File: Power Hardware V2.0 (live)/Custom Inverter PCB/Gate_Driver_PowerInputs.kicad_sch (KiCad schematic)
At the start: 22 parts, among them J1 1714971, J2 1714971, J3 1714968, J7 1714971, J8 1714971, K2 1-1393210-3, U1 DRV8300DIPWR

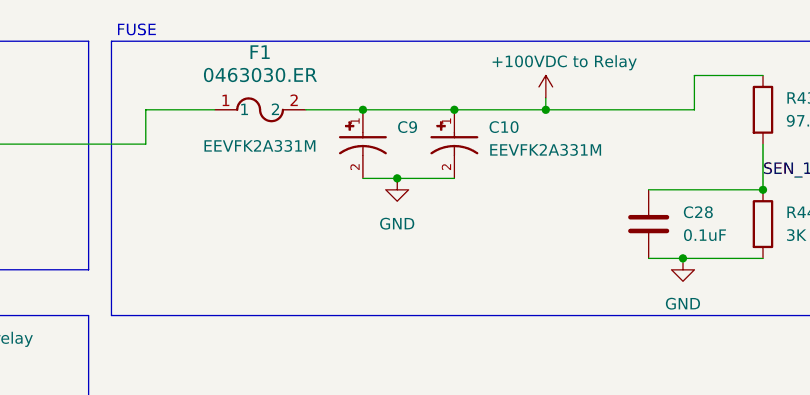
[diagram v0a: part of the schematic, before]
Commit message: footprint fixes
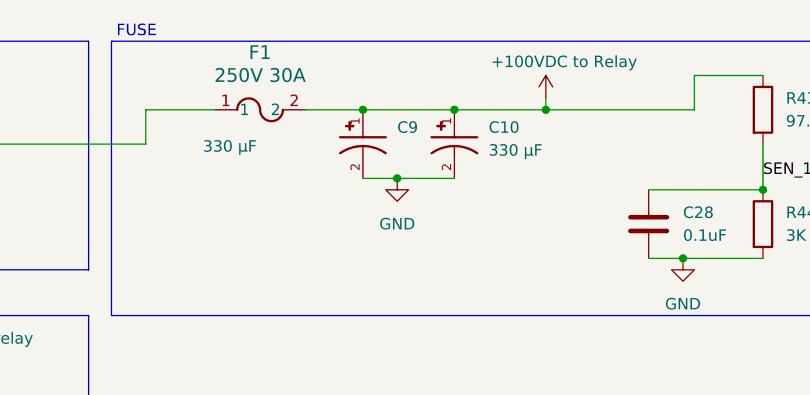
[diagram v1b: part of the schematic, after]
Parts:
- C10, C9: value EEVFK2A331M -> 330 µF; Part Number (none) -> EEVFK2A331M
- F1: value 0463030.ER -> 250V 30A; footprint 0463030ERFUSE:FUSE_0463_LTF-L -> 0463030_ER:FUSE_0463_LTF-M
- J3: footprint 1714968:PHOENIX_1714968 -> PHOENIX_1714968:PHOENIX_1714968
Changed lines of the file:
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@@
 			)
 		)
-		(property "Value" "EEVFK2A331M"
+		(property "Value" "330 µF"
 			(at 63.5 26.924 90)
 			(effects
@@
 			)
 		)
-		(property "Datasheet" ""
+		(property "Datasheet" "https://industrial.panasonic.com/cdbs/www-data/pdf/RDE0000/ABA0000C1181.pdf"
 			(at 81.28 25.4 0)
 			(effects
@@
 			)
 		)
-		(property "Part Number" ""
+		(property "Part Number" "EEVFK2A331M"
 			(at 81.28 25.4 0)
 			(effects
@@
 			)
 		)
-		(property "Value" "0463030.ER"
+		(property "Value" "250V 30A"
 			(at 69.85 19.05 0)
 			(effects
@@
 			)
 		)
-		(property "Footprint" "0463030ERFUSE:FUSE_0463_LTF-L"
+		(property "Footprint" "0463030_ER:FUSE_0463_LTF-M"
 			(at 64.77 22.86 0)
 			(effects
@@
 			)
 		)
-		(property "Footprint" "1714968:PHOENIX_1714968"
+		(property "Footprint" "PHOENIX_1714968:PHOENIX_1714968"
 			(at 265.43 90.17 0)
 			(effects
@@
 			)
 		)
-		(property "Value" "EEVFK2A331M"
+		(property "Value" "330 µF"
 			(at 95.25 27.3665 90)
 			(effects
@@
 			)
 		)
-		(property "Datasheet" ""
+		(property "Datasheet" "https://industrial.panasonic.com/cdbs/www-data/pdf/RDE0000/ABA0000C1181.pdf"
 			(at 91.44 25.4 0)
 			(effects
@@
 			)
 		)
-		(property "Part Number" ""
+		(property "Part Number" "EEVFK2A331M"
 			(at 91.44 25.4 0)
 			(effects

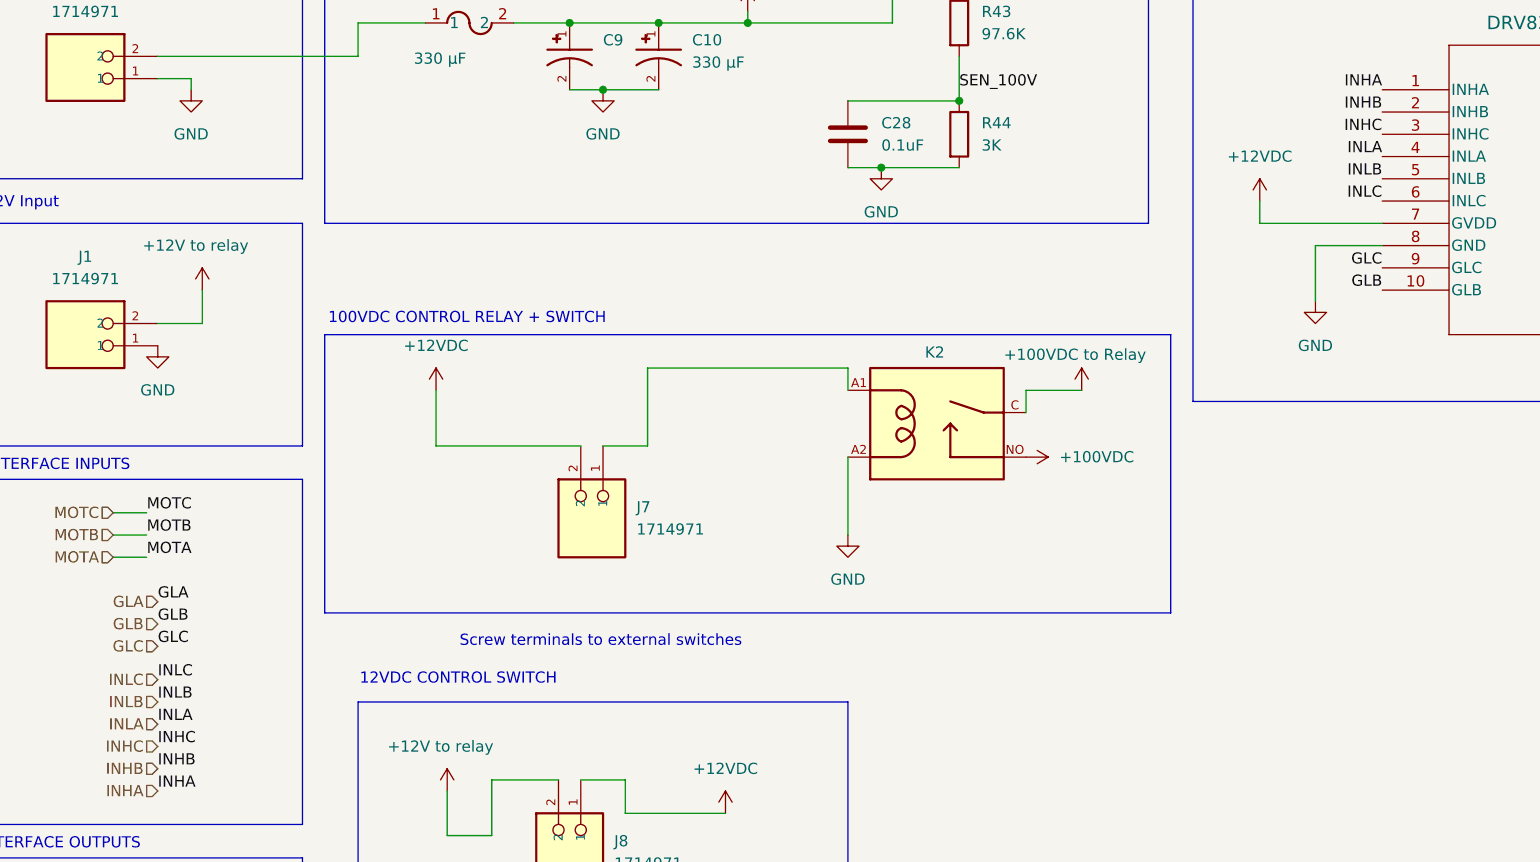
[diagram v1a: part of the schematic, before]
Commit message: Pcb layout and tracing
changed footprint file for current sense ic
did layout and tracing for pcb
created bom
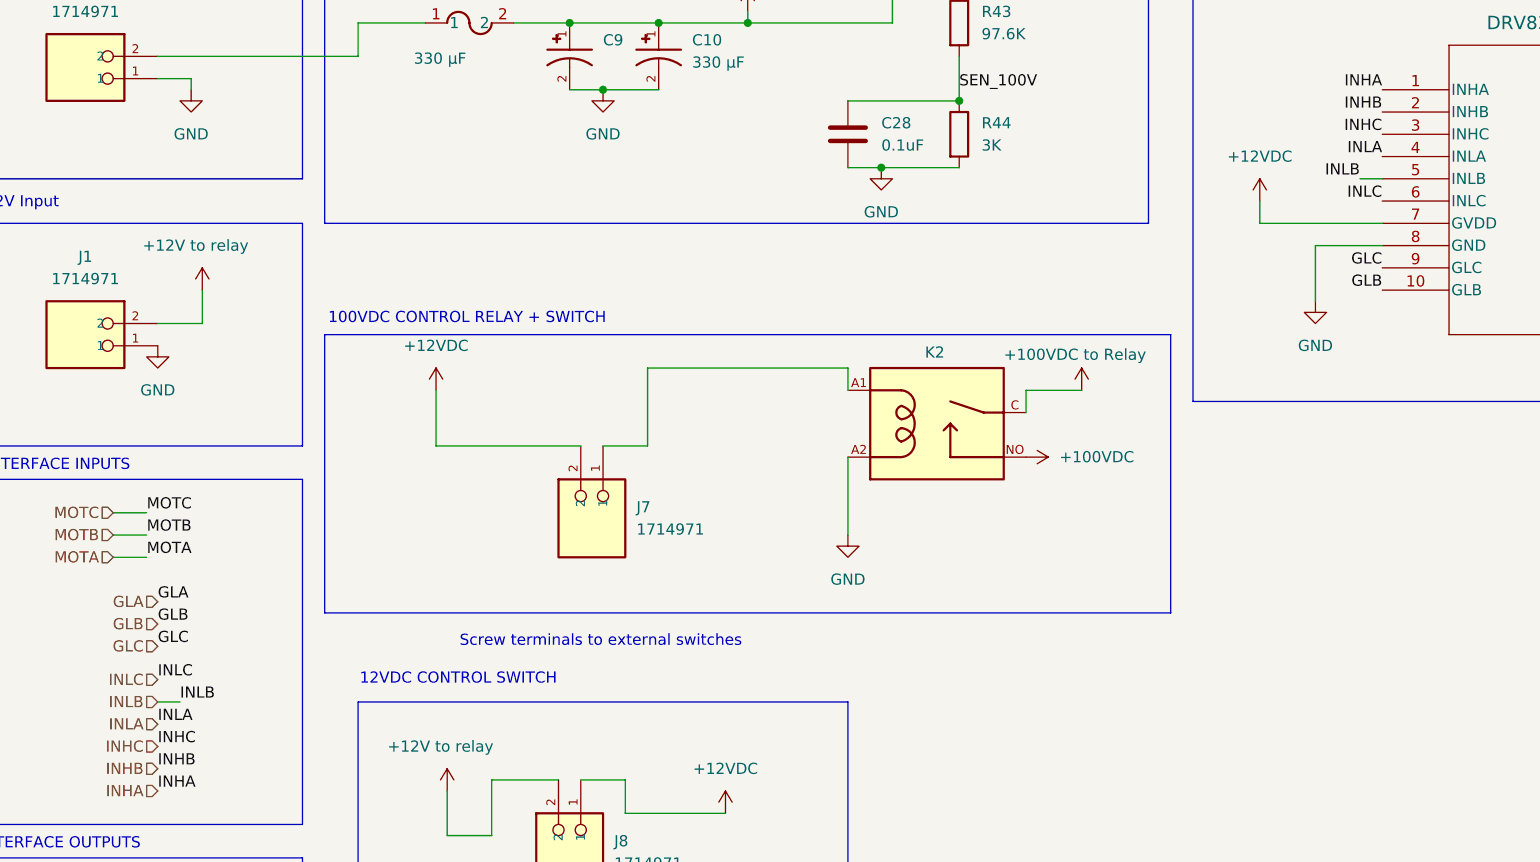
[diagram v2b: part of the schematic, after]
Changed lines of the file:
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@@
+	(wire
+		(pts
+			(xy 171.45 40.64) (xy 173.99 40.64)
+		)
+		(stroke
+			(width 0)
+			(type default)
+		)
+	)
 	(wire
 		(pts
@@
 		(pts
 			(xy 25.4 143.51) (xy 34.29 143.51)
+		)
+		(stroke
+			(width 0)
+			(type default)
+		)
+	)
+	(wire
+		(pts
+			(xy 36.83 100.33) (xy 34.29 100.33)
 		)
 		(stroke
@@
 	)
 	(label "INLB"
-		(at 173.99 40.64 180)
+		(at 171.45 40.64 180)
 		(effects
 			(font
@@
 	)
 	(label "INLB"
-		(at 34.29 100.33 0)
-		(effects
-			(font
+		(at 36.83 100.33 0)
+		(effects
+			(font

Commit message: PCB Fixes
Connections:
- net PVDD: now reaches F1.1, J2.2
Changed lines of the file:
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@@
+	(wire
+		(pts
+			(xy 39.37 59.69) (xy 34.29 59.69)
+		)
+		(stroke
+			(width 0)
+			(type default)
+		)
+	)
 	(wire
 		(pts
@@
 	(label "SHC"
 		(at 271.78 55.88 0)
+		(effects
+			(font
+				(size 1.27 1.27)
+			)
+			(justify left bottom)
+		)
+	)
+	(label "PVDD"
+		(at 43.18 26.67 0)
 		(effects
 			(font
@@
 	(symbol
 		(lib_id "power:GND")
-		(at 34.29 59.69 0)
+		(at 39.37 59.69 0)
 		(unit 1)
 		(exclude_from_sim no)
@@
 		(fields_autoplaced yes)
 		(property "Reference" "#PWR013"
-			(at 34.29 66.04 0)
+			(at 39.37 66.04 0)
 			(effects
 				(font
@@
 		)
 		(property "Value" "GND"
-			(at 34.29 64.77 0)
+			(at 39.37 64.77 0)
 			(effects
 				(font
@@
 		)
 		(property "Footprint" ""
-			(at 34.29 59.69 0)
+			(at 39.37 59.69 0)
 			(effects
 				(font
@@
 		)
 		(property "Datasheet" ""
-			(at 34.29 59.69 0)
+			(at 39.37 59.69 0)
 			(effects
 				(font
@@
 		)
 		(property "Description" "Power symbol creates a global label with name \"GND\" , ground"
-			(at 34.29 59.69 0)
-			(effects
-				(font
+			(at 39.37 59.69 0)
+			(effects
+				(font
